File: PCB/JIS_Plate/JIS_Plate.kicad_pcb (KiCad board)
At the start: 2 copper layers, 285 x 94.6 mm, 93 parts, among them SW10 EC_SW, SW11 EC_SW, SW12 EC_SW, SW13 EC_SW, SW14 EC_SW, SW15 EC_SW, SW17 EC_SW, SW18 EC_SW, SW19 EC_SW, SW2 EC_SW, SW20 EC_SW, SW21 EC_SW, SW22 EC_SW, SW23 EC_SW, SW24 EC_SW, SW25 EC_SW, SW26 EC_SW, SW27 EC_SW, SW28 EC_SW, SW29 EC_SW, SW3 EC_SW, SW30 EC_SW, SW32 ISO_Enter, SW34 EC_SW, SW35 EC_SW, SW36 EC_SW, SW37 EC_SW, SW38 EC_SW, SW39 EC_SW, SW4 EC_SW, SW40 EC_SW, SW41 EC_SW, SW42 EC_SW, SW43 EC_SW, SW44 EC_SW, SW45 ISO_|, SW5 EC_SW, SW50 EC_SW, SW51 EC_SW, SW52 EC_SW, SW53 EC_SW, SW54 EC_SW, SW55 EC_SW, SW56 EC_SW, SW57 EC_SW, SW58 EC_SW, SW59 EC_SW, SW6 EC_SW, SW63 EC_SW, SW64 EC_SW, SW65 EC_SW, SW66 EC_SW, SW7 EC_SW, SW70 EC_SW, SW72 EC_SW, SW73 EC_SW, SW8 EC_SW, SW9 EC_SW

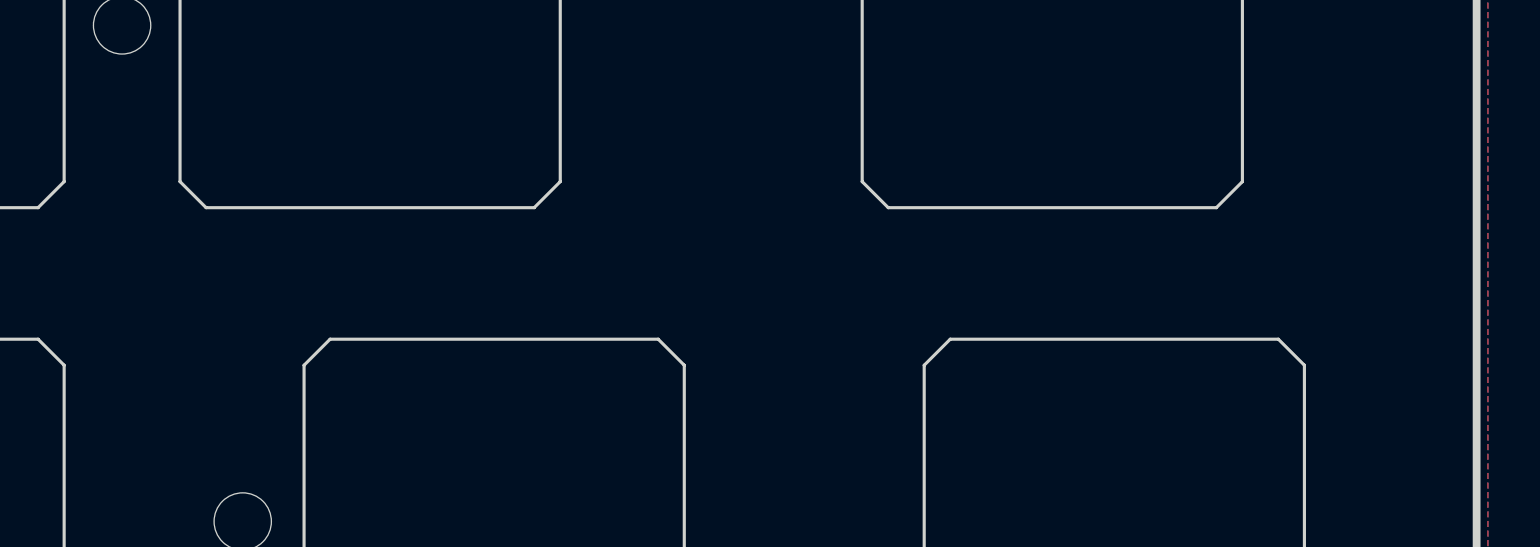
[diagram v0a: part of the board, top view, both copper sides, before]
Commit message: REV 1.1 upload
Some changes include:
- reassign of pins to avoid compiler problem
- changes in silkscreen
- moved to different USB port for better availability
- added 7U hhkb plate
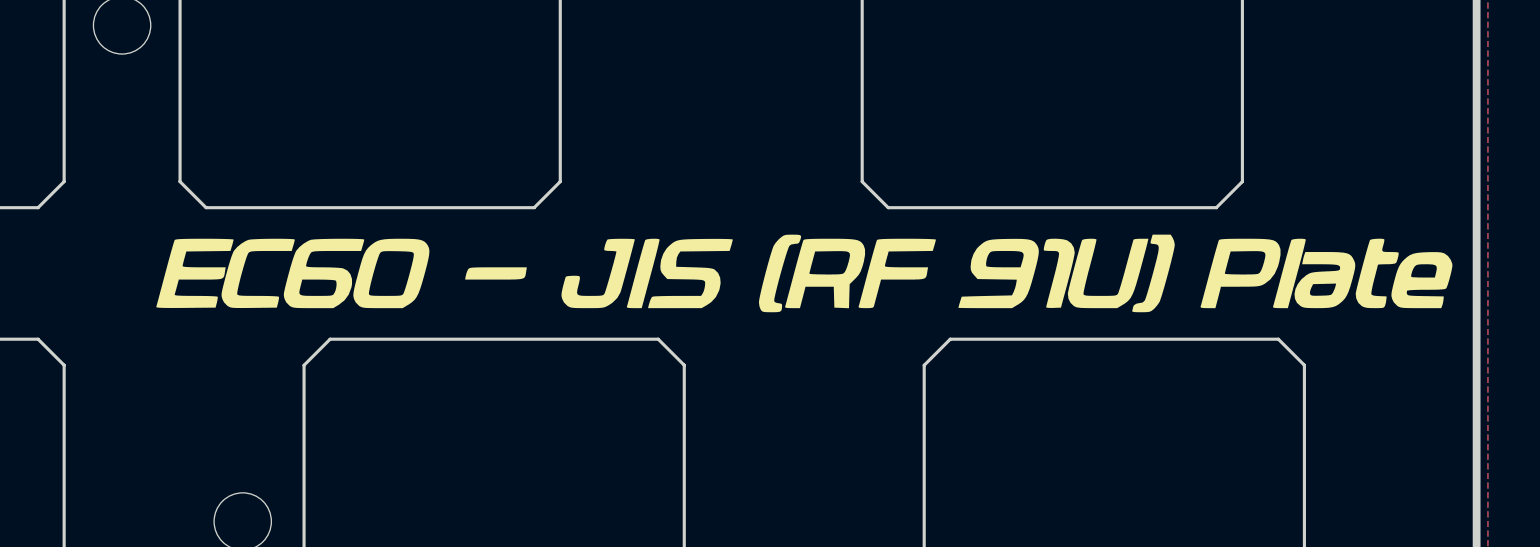
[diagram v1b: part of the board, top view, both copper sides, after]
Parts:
- added G***: LOGO, LOGO, F.Cu at (331.0, 179.8)
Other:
- board text removed: "EC60 JIS Plate (RF 91U)"
